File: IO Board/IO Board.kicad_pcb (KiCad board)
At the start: 2 copper layers, 49.5 x 55.3 mm, 8 parts, among them J1 Conn_01x07_Female

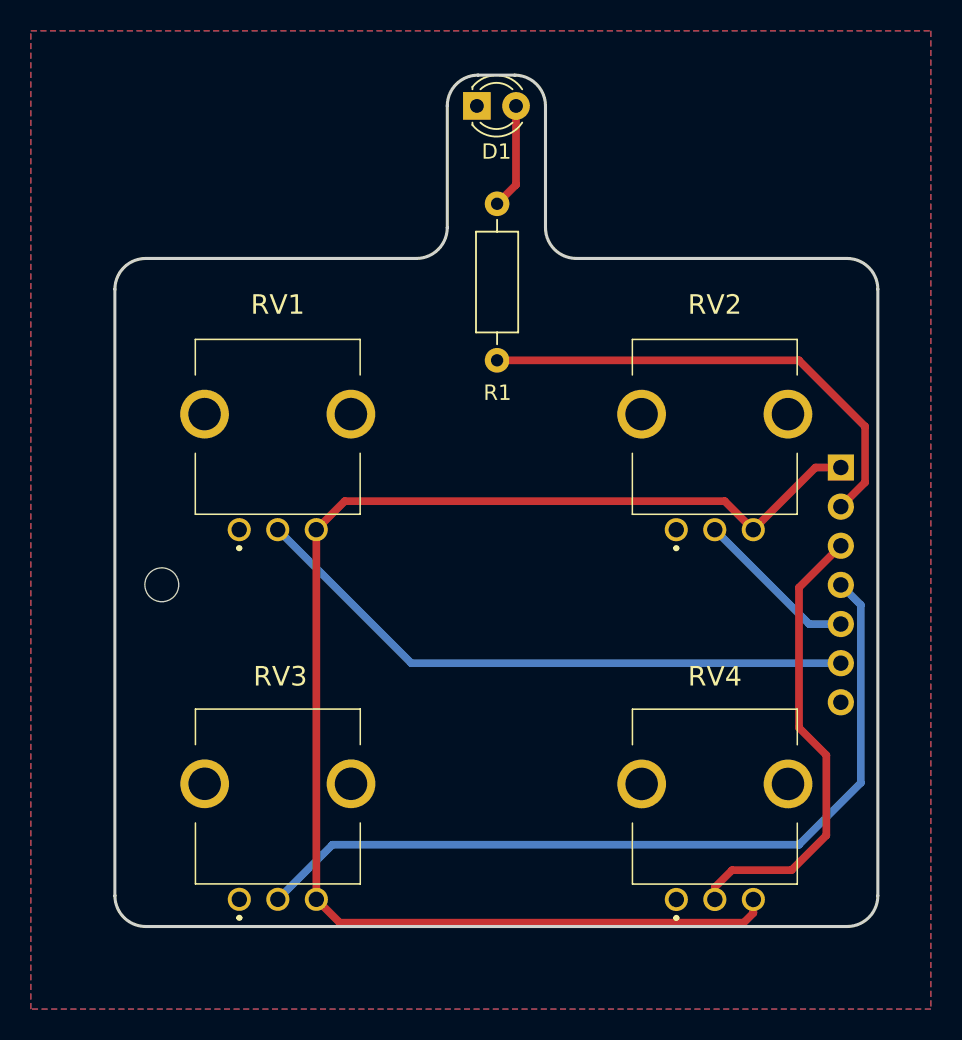
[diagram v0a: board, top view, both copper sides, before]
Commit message: Move components to make space for the pedal plug
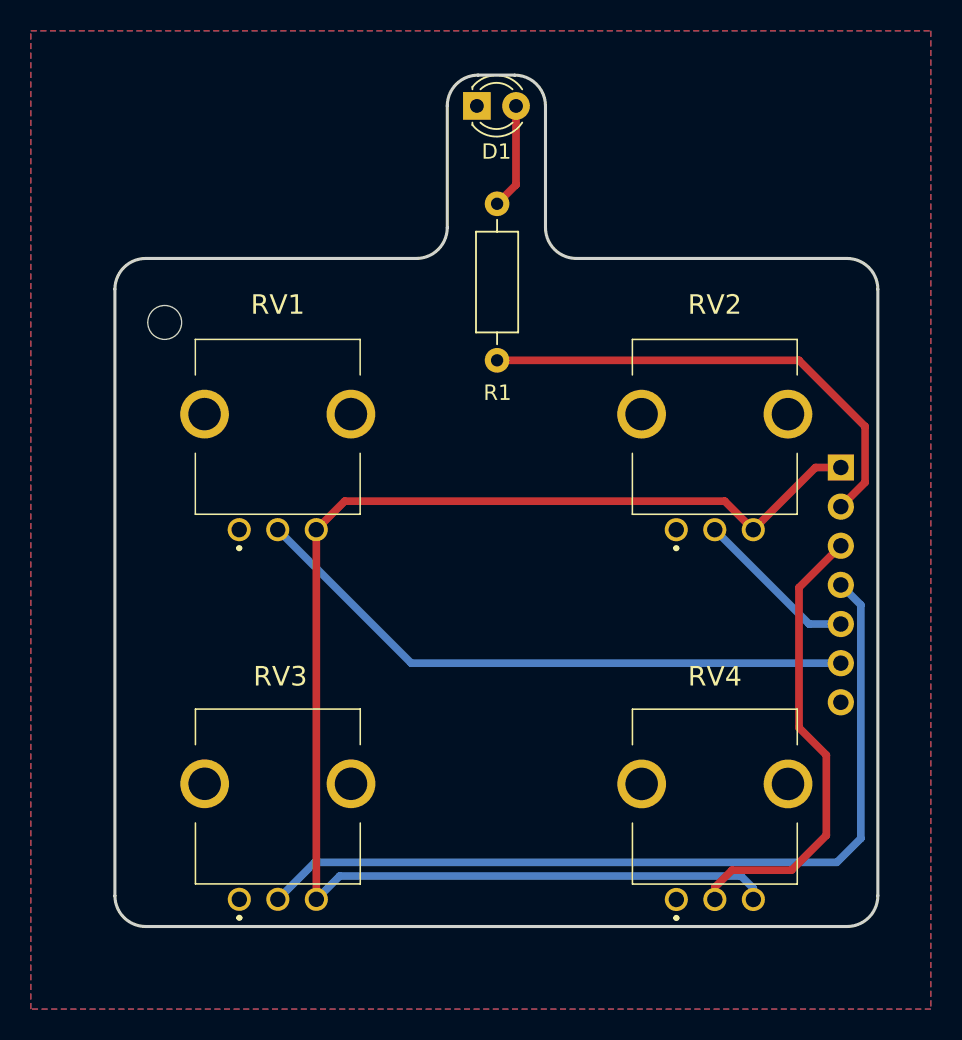
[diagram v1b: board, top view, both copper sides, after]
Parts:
- moved H1 17.0 mm to (194.1, 72.3)
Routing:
- net POT3: track 54.4 -> 56.5 mm

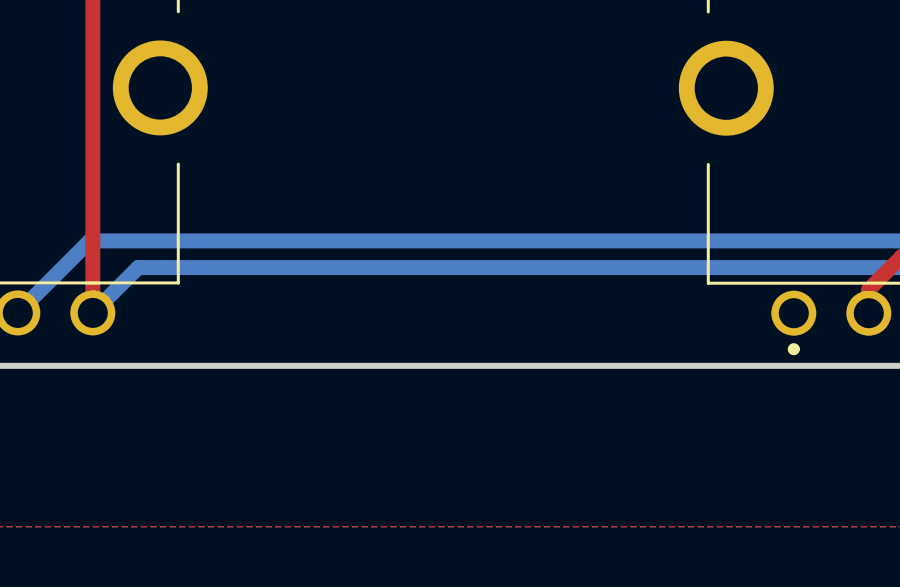
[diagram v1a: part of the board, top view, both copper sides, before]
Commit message: Finish adding the expression pedal. New release.
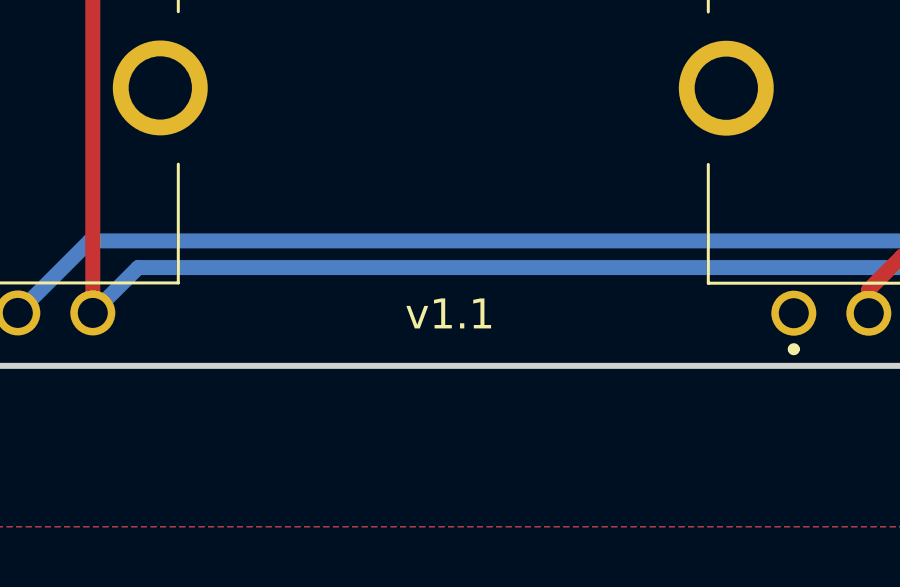
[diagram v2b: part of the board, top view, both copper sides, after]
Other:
- board text added: "v1.1"
